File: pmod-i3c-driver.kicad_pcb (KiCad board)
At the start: 4 copper layers, 75 x 36.5 mm, 80 parts, among them J1 PinSocket_2x12_P2.54mm_Drill1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, J2 PinSocket_2x6_P2.54mm_Drill1.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, J3 JST_SH_1x4_SM04B-SRSS-TB-LF-SN, J4 USB-C_CUI_UJC-HP-3-SMT-TR, J5 PinHeader_1x3_P2.54mm_Drill1.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, J6 PinHeader_1x3_P2.54mm_Drill1.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, J7 PinHeader_2x10_P1.27mm_SMD, Q1 DMC31D5UDJ, Q2 DMC31D5UDJ, Q3 DMC2400UV-7, Q4 DMC2400UV-7, Q5 DMG1012T-7, U1 TPS7A0518P_SOT23-5, U2 SN74LVC1G240_SC70, U3 SN74LVC1G240_SC70, U4 TLV70033_SC70

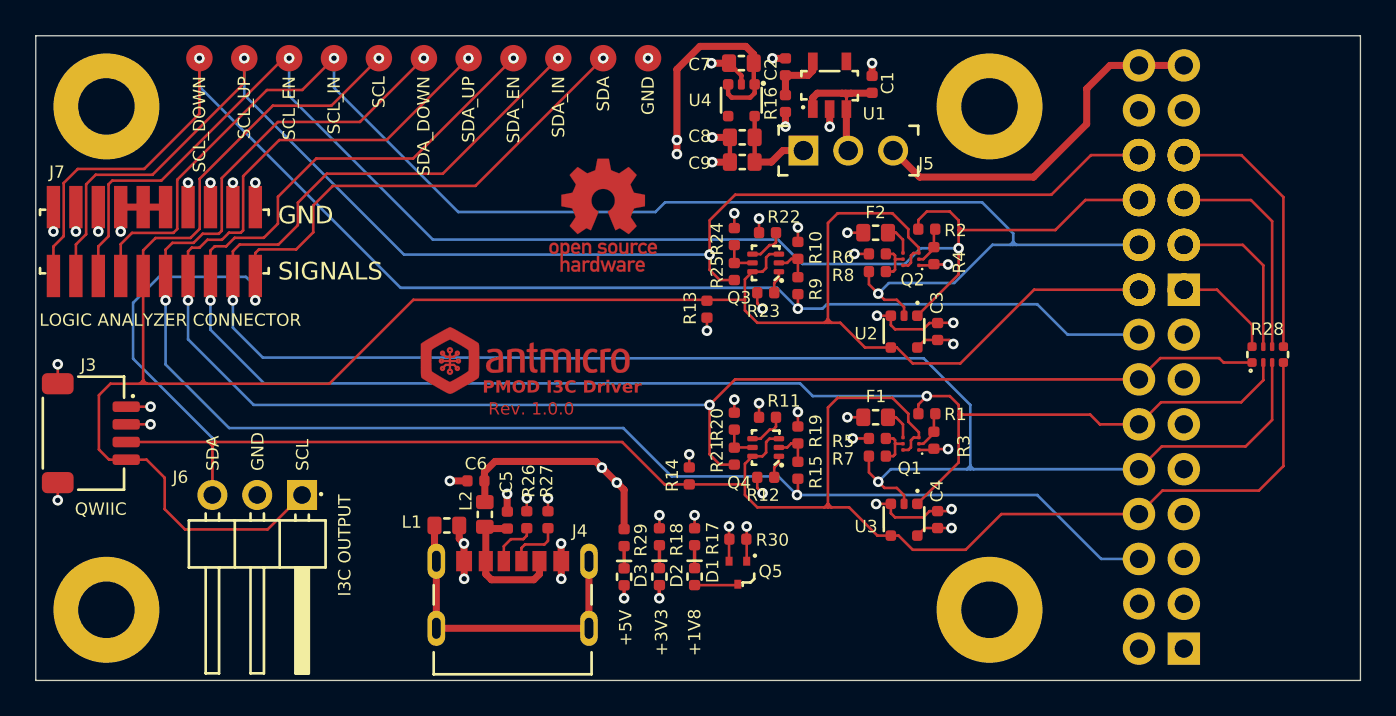
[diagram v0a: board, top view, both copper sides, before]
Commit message: [#80692] Update footprints, clean ERC, bump rev to 1.0.1
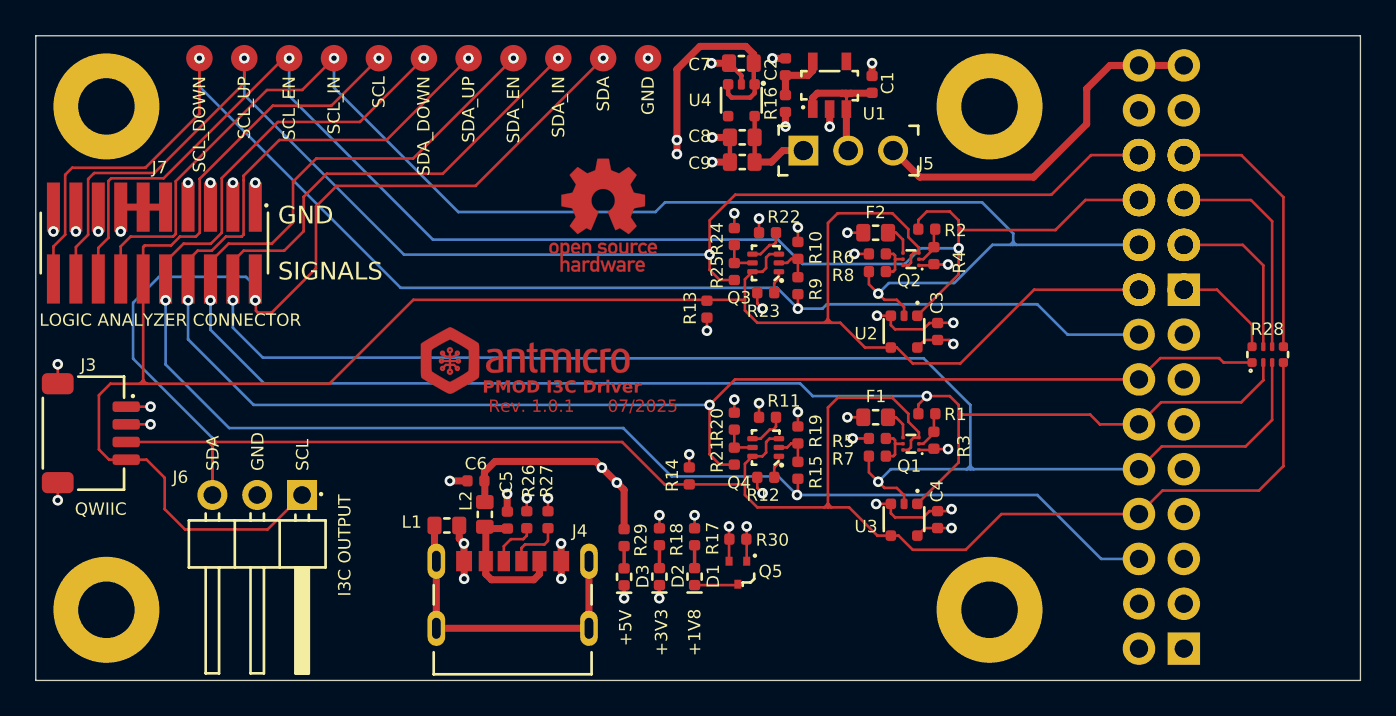
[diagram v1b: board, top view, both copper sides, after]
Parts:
- J7: value PinHeader_2x10_P1.27mm_SMD -> PinHeader_2x10_P1.27mm_SMD_Latch; footprint antmicro-footprints:PinHeader_2x10_P1.27mm_SMD -> antmicro-footprints:PinHeader_2x10_P1.27mm_SMD_Latch
- moved J7 3.14 mm to (136.1, 96.0), turned to -90 degrees
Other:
- board text added: "07/2025"
